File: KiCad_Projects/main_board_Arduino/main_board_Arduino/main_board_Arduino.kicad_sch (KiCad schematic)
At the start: 41 parts

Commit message: 基板データの更新
メイン基板データの更新
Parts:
- removed C? (x8): C_Small, symbol Device:C_Small
- removed C?: C, symbol Device:C
- removed R? (x8): 100k, symbol Device:R
- removed SW?: SW_Push, symbol Switch:SW_Push
- removed U? (x8): TSSP58038, symbol ir_sensor:TSSP58038
- removed U?: open_mv, symbol open_mv:open_mv
- added C? (x11): C_Small, Capacitor_THT:C_Disc_D3.8mm_W2.6mm_P2.50mm, symbol Device:C_Small
- added C?: C, Capacitor_THT:CP_Radial_D5.0mm_P2.50mm, symbol Device:C
- added D?: D, symbol Device:D
- added J?: Conn_01x02_Female, symbol Connector:Conn_01x02_Female
- added J?: Conn_01x11_Female, symbol Connector:Conn_01x11_Female
- added R? (x3): 33k, Resistor_THT:R_Axial_DIN0204_L3.6mm_D1.6mm_P5.08mm_Horizontal, symbol Device:R
- added R? (x8): 100k, Resistor_THT:R_Axial_DIN0204_L3.6mm_D1.6mm_P5.08mm_Horizontal, symbol Device:R
- added SW?: SW_Push, Button_Switch_THT:SW_PUSH_6mm_H5mm, symbol Switch:SW_Push
- added U? (x8): TSSP58038, Lib:TSSP58038_IR, symbol ir_sensor:TSSP58038
- added U?: open_mv, Lib:OpenMV, symbol open_mv:open_mv
- R?: value R -> 10k
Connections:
- net +3V3: now also U?.44 (3.3v), U?.45 (3.3v), J?.2 (Pin_2), U?.2 (Vin), U?.2 (Vin), U?.2 (Vin), U?.2 (Vin), U?.2 (Vin), U?.2 (Vin), U?.2 (Vin), U?.2 (Vin)
- net +5V: now also U?.42 (5v), U?.43 (5v), C?.1, U?.9 (vin)
- net AD3: now also C?.1, R?.2
- net AD4: now also C?.1, R?.2
- net AD5: now also C?.1, R?.2
- net GND: now also U?.40 (gnd), U?.41 (gnd), C?.1, C?.1, C?.1, C?.1, C?.2, C?.2, C?.2, C?.2, C?.2, C?.2, C?.2, C?.2, J?.1 (Pin_1), J?.1 (Pin_1), SW?.2, U?.1 (GND), U?.1 (GND), U?.1 (GND), U?.1 (GND), U?.1 (GND), U?.1 (GND), U?.1 (GND), U?.1 (GND), U?.8 (gnd)
- net IR1: now also C?.1, R?.1
- net IR2: now also C?.1, R?.1
- net IR3: now also C?.1, R?.1
- net IR4: now also C?.1, R?.1
- net IR5: now also C?.2, R?.2
- net IR6: now also C?.2, R?.2
- net IR7: now also C?.2, R?.2
- net IR8: now also C?.2, R?.2
- net SW2: now also J?.4 (Pin_4)
- net SCLK: now reaches U?.21 (d37)
- net SCLK: now also J?.8 (Pin_8)
- net +7.5V: now reaches U?.38 (vin)
- net +7.5V: now also U?.39 (vin), D?.1 (K)
- new net: R?.1, U?.11 (seru02)
- new net: R?.1, U?.0 (OUT) (x4)
- new net: R?.2, U?.0 (OUT) (x4)
- new net: R?.1, U?.10 (seru01)
- new net: R?.1, U?.12 (seru03)
- new net: SW?.1, U?.15 (rst)
- new net: D?.2 (A), J?.2 (Pin_2)
- new net CS: J?.11 (Pin_11)
- new net RE: J?.10 (Pin_10)
- new net SDI: J?.7 (Pin_7)
- new net SW1: J?.3 (Pin_3)
- new net SW3: J?.5 (Pin_5)
- new net SW4: J?.6 (Pin_6)
- no-connect marks 0 -> 10
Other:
- moved on the sheet: D?, J?, R?

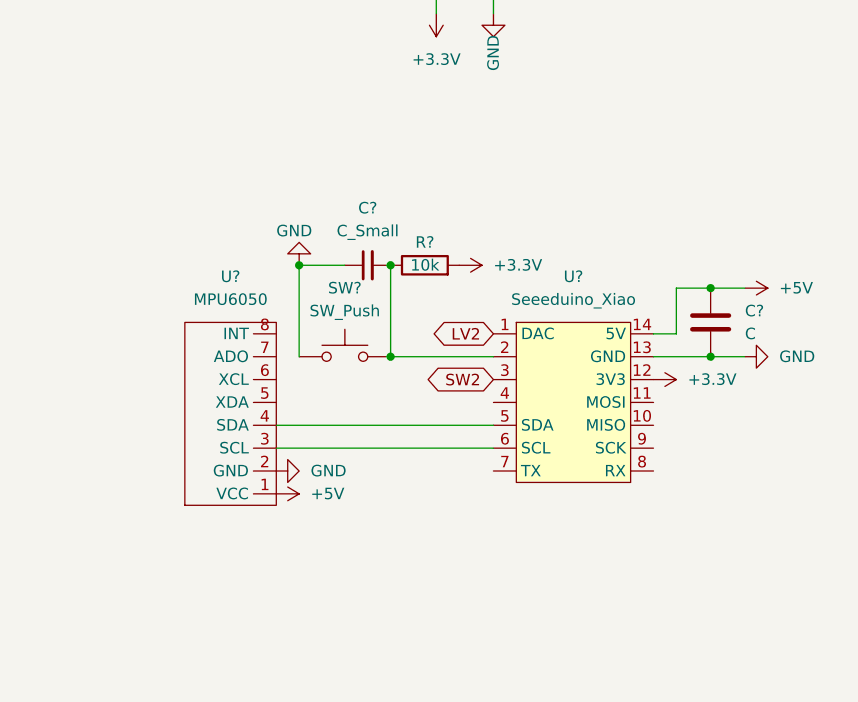
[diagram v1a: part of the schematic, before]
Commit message: 基板データの更新
IO基板のCNCバージョン作成
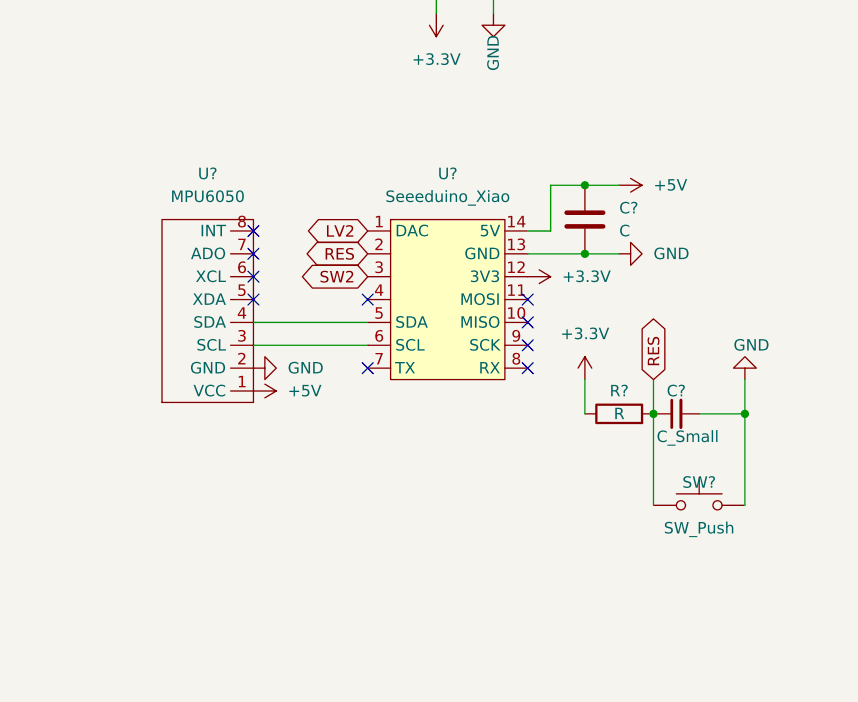
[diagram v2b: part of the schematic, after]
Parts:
- removed C?: C, symbol Device:C
- removed C?: C_Small, symbol Device:C_Small
- removed R?: 10k, symbol Device:R
- removed SW?: SW_Push, symbol Switch:SW_Push
- removed U?: MPU6050, symbol mpu6050:MPU6050
- removed U?: Seeeduino_Xiao, symbol seeeduino_xiao:Seeeduino_Xiao
- added C?: C_Small, Capacitor_THT:C_Disc_D3.8mm_W2.6mm_P2.50mm, symbol Device:C_Small
- added C?: C, Capacitor_THT:CP_Radial_D5.0mm_P2.50mm, symbol Device:C
- added R?: R, Resistor_THT:R_Axial_DIN0204_L3.6mm_D1.6mm_P5.08mm_Horizontal, symbol Device:R
- added SW?: SW_Push, Button_Switch_THT:SW_PUSH_6mm_H5mm, symbol Switch:SW_Push
- added U?: MPU6050, Lib:MPU6050, symbol mpu6050:MPU6050
- added U?: Seeeduino_Xiao, Lib:seeeduinoXIAO, symbol seeeduino_xiao:Seeeduino_Xiao
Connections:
- net +3V3: now also R?.1, U?.12 (3V3)
- net +5V: now also C?.1, U?.1 (VCC), U?.14 (5V)
- net GND: now also C?.2, C?.2, SW?.2, U?.13 (GND), U?.2 (GND)
- net LV2: now also U?.1 (DAC)
- net SW2: now also U?.3
- new net: U?.3 (SCL), U?.6 (SCL)
- new net: U?.4 (SDA), U?.5 (SDA)
- new net RES: C?.1, R?.2, SW?.1, U?.2
- no-connect marks 10 -> 20
